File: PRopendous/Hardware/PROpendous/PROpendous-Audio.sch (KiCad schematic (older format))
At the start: 25 parts, among them M1 ELECTRET_MIC, U7 Video, U8 Headphones, U9 Line

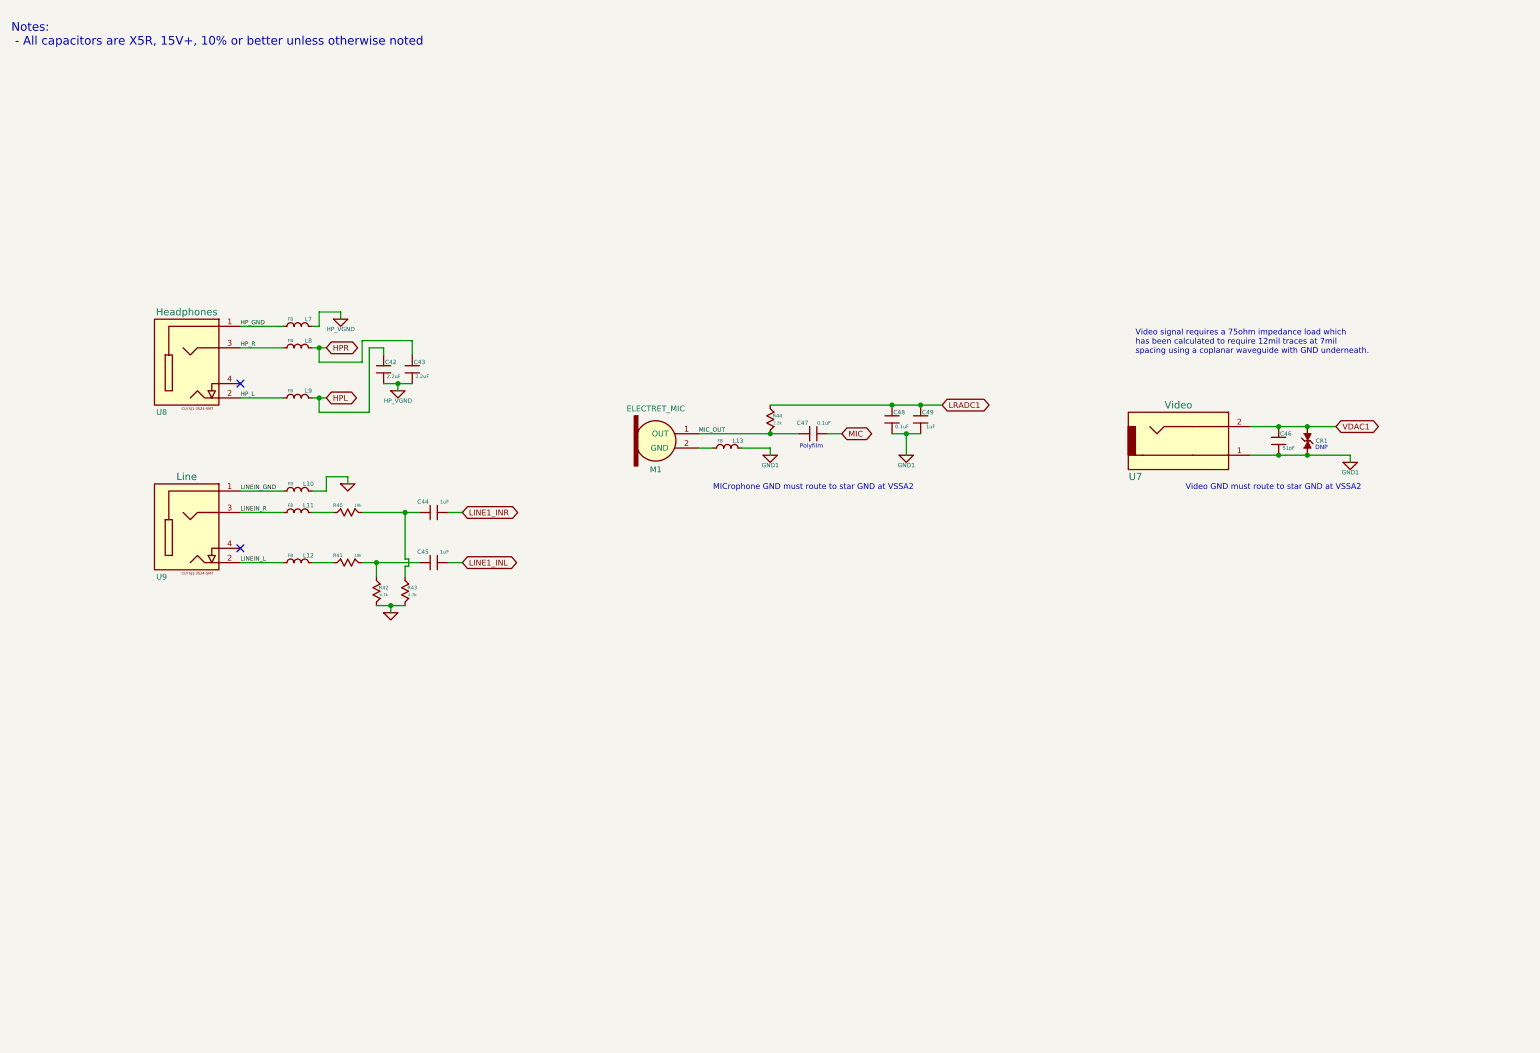
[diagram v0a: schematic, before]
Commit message: Updated PROpendous Project.  PCB layout is nearing completion.
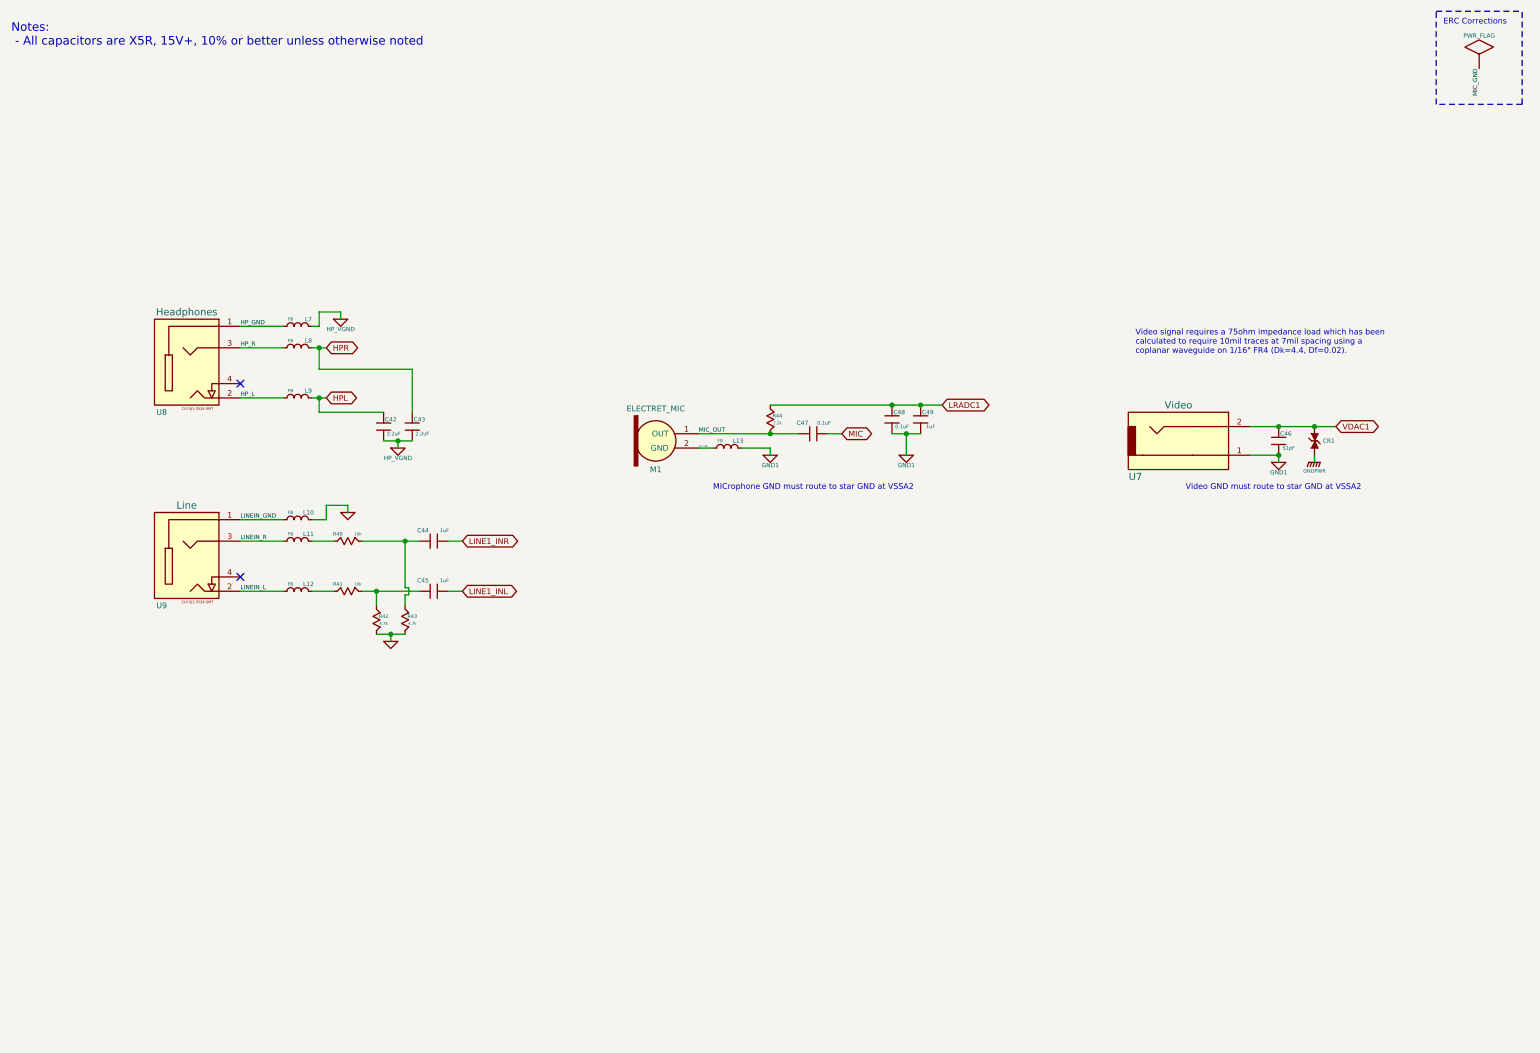
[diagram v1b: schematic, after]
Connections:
- net GND1: no longer CR1.1 (cathode)
- net MIC_GND: now reaches L13.2 (B), M1.2 (GND)
- new net GNDPWR: CR1.1 (cathode)
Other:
- note added: "ERC Corrections"
- note added: "Video signal requires a 75ohm impedance load which has been\ncalculated to require 10mil traces at 7mil spacing using a\ncoplanar waveguide on 1/16" FR4 (Dk=4.4, Df=0.02)."
- note removed: "DNP"
- note removed: "Polyfilm"
- note removed: "Video signal requires a 75ohm impedance load which\nhas been calculated to require 12mil traces at 7mil\nspacing using a coplanar waveguide with GND underneath."
- moved on the sheet: C42, C43, C44, C45, CR1, L10, L11, L12, R40, R41, R42, R43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

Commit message: First revision of i.MX233-based PROpendous board is complete.
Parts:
- added C79, C80: 0.1uF, symbol C_MINI
- added C81: 10uF, symbol C_MINI
- added IC7: MMA7455, symbol MMA745X
- added TP10: CONN_1, symbol CONN_1
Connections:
- net labels added: I2C_SCL-GPMI_RDY2-AUART1_TX, I2C_SDA-GPMI_CE2n-AUART1_RX, VDDIO_3V3
- wire segments 49 -> 60
- no-connect marks 2 -> 7
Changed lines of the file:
@@
-EESchema Schematic File Version 2  date 25/04/2010 07:03:32
+EESchema Schematic File Version 2  date 26/04/2010 13:13:01
 LIBS:opendous
 LIBS:device
@@
 Sheet 6 8
 Title "PROpendous"
-Date "25 apr 2010"
+Date "26 apr 2010"
 Rev "1.0"
 Comp "Opendous Inc. (www.opendous.org)"
@@
 Comment4 "www.PROpendous.org"
 $EndDescr
-Wire Wire Line
-	3450 3300 3450 3000
-Wire Wire Line
-	3450 3000 2800 3000
-Connection ~ 2800 2850
-Wire Wire Line
-	2800 3000 2800 2850
+Text GLabel 6600 7650 2    40   BiDi ~ 0
+MIC_OUT
+Text GLabel 6600 7550 2    40   BiDi ~ 0
+MIC_GND
+Text Label 6600 7550 2    30   ~ 0
+MIC_GND
+Text Label 6600 7650 2    30   ~ 0
+MIC_OUT
+Wire Wire Line
+	6150 6250 6050 6250
+Connection ~ 5350 5800
+Wire Wire Line
+	6050 6100 6050 5800
+Wire Wire Line
+	5300 7250 5300 7300
+Wire Wire Line
+	5250 6700 5350 6700
+Wire Wire Line
+	5300 6700 5300 6750
+Connection ~ 5300 6700
+Wire Wire Line
+	5300 5800 5300 5750
+Connection ~ 5300 5800
+Wire Wire Line
+	5500 7050 5100 7050
+Connection ~ 5300 7050
+Wire Wire Line
+	5500 7250 5100 7250
+Connection ~ 5300 7250
+Wire Wire Line
+	5300 7000 5300 7050
+Connection ~ 2800 3200
+Wire Wire Line
+	3250 3300 2800 3300
+Wire Wire Line
+	2800 3300 2800 3200
+Connection ~ 9750 3400
+Wire Wire Line
+	9300 3400 9900 3400
+Connection ~ 9500 3600
+Wire Wire Line
+	9500 3650 9500 3600
+Connection ~ 6800 3250
+Wire Wire Line
+	7150 3250 5950 3250
+Wire Wire Line
+	7000 3450 6800 3450
+Wire Wire Line
+	5550 3550 5450 3550
+Connection ~ 5950 3450
+Wire Wire Line
+	5450 3450 6150 3450
+Wire Wire Line
+	9500 3600 9300 3600
+Wire Wire Line
+	3700 4550 3800 4550
+Connection ~ 3300 4850
+Wire Wire Line
+	3300 4900 3300 4850
+Wire Wire Line
+	3000 4000 3000 3950
+Wire Wire Line
+	3000 3950 2850 3950
+Wire Wire Line
+	2850 3950 2850 4050
+Wire Wire Line
+	2850 4050 2750 4050
+Connection ~ 3200 4550
+Wire Wire Line
+	3200 4650 3200 4550
+Wire Wire Line
+	3500 4200 3100 4200
+Wire Wire Line
+	2750 4200 2900 4200
+Wire Wire Line
+	2250 4050 2550 4050
+Wire Wire Line
+	2250 4550 2550 4550
+Wire Wire Line
+	2850 2850 2750 2850
+Connection ~ 3350 3500
+Wire Wire Line
+	3350 3550 3350 3500
+Wire Wire Line
+	2250 3200 2550 3200
+Wire Wire Line
+	2250 2700 2550 2700
+Wire Wire Line
+	2250 2850 2550 2850
+Wire Wire Line
+	3250 3500 3450 3500
+Wire Wire Line
+	2750 2700 2800 2700
+Wire Wire Line
+	2800 2700 2800 2600
+Wire Wire Line
+	2800 2600 2950 2600
+Wire Wire Line
+	2950 2600 2950 2650
+Wire Wire Line
+	2750 3200 2850 3200
+Wire Wire Line
+	2550 4200 2250 4200
+Wire Wire Line
+	2750 4550 2900 4550
+Wire Wire Line
+	3500 4550 3100 4550
+Wire Wire Line
+	3400 4200 3400 4525
+Connection ~ 3400 4200
+Wire Wire Line
+	3400 4525 3425 4525
+Wire Wire Line
+	3425 4525 3425 4575
+Wire Wire Line
+	3425 4575 3400 4575
+Wire Wire Line
+	3400 4575 3400 4650
+Wire Wire Line
+	3200 4850 3400 4850
+Wire Wire Line
+	3700 4200 3800 4200
+Wire Wire Line
+	6450 3450 6350 3450
+Wire Wire Line
+	5750 3550 5950 3550
+Wire Wire Line
+	5950 3550 5950 3600
+Wire Wire Line
+	6900 3600 6900 3450
+Connection ~ 6900 3450
+Connection ~ 7000 3250
+Wire Wire Line
+	9750 3650 9750 3600
+Connection ~ 9500 3400
+Wire Notes Line
+	10600 500  11200 500
+Wire Notes Line
+	10600 500  10600 1150
+Wire Notes Line
+	10600 1150 11200 1150
 Wire Notes Line
 	11200 1150 11200 500
-Wire Notes Line
-	11200 1150 10600 1150
-Wire Notes Line
-	10600 1150 10600 500
-Wire Notes Line
-	10600 500  11200 500
-Connection ~ 9500 3400
-Wire Wire Line
-	9750 3650 9750 3600
-Connection ~ 7000 3250
-Connection ~ 6900 3450
-Wire Wire Line
-	6900 3600 6900 3450
-Wire Wire Line
-	5950 3600 5950 3550
-Wire Wire Line
-	5950 3550 5750 3550
-Wire Wire Line
-	6450 3450 6350 3450
-Wire Wire Line
-	3700 4200 3800 4200
-Wire Wire Line
-	3200 4850 3400 4850
-Wire Wire Line
-	3400 4650 3400 4575
-Wire Wire Line
-	3400 4575 3425 4575
-Wire Wire Line
-	3425 4575 3425 4525
-Wire Wire Line
-	3425 4525 3400 4525
-Connection ~ 3400 4200
-Wire Wire Line
-	3400 4525 3400 4200
-Wire Wire Line
-	3500 4550 3100 4550
-Wire Wire Line
-	2750 4550 2900 4550
-Wire Wire Line
-	2550 4200 2250 4200
-Wire Wire Line
-	2750 3200 2850 3200
-Wire Wire Line
-	2950 2650 2950 2600
-Wire Wire Line
-	2950 2600 2800 2600
-Wire Wire Line
-	2800 2600 2800 2700
-Wire Wire Line
-	2800 2700 2750 2700
-Wire Wire Line
-	3250 3500 3450 3500
-Wire Wire Line
-	2250 2850 2550 2850
-Wire Wire Line
-	2250 2700 2550 2700
-Wire Wire Line
-	2250 3200 2550 3200
-Wire Wire Line
-	3350 3550 3350 3500
-Connection ~ 3350 3500
-Wire Wire Line
-	2850 2850 2750 2850
-Wire Wire Line
-	2250 4550 2550 4550
-Wire Wire Line
-	2250 4050 2550 4050
-Wire Wire Line
-	2750 4200 2900 4200
-Wire Wire Line
-	3500 4200 3100 4200
-Wire Wire Line
-	3200 4650 3200 4550
-Connection ~ 3200 4550
-Wire Wire Line
-	2750 4050 2850 4050
-Wire Wire Line
-	2850 4050 2850 3950
-Wire Wire Line
-	2850 3950 3000 3950
-Wire Wire Line
-	3000 3950 3000 4000
-Wire Wire Line
-	3300 4900 3300 4850
-Connection ~ 3300 4850
-Wire Wire Line
-	3700 4550 3800 4550
-Wire Wire Line
-	9300 3600 9500 3600
-Wire Wire Line
-	5450 3450 6150 3450
-Connection ~ 5950 3450
-Wire Wire Line
-	5550 3550 5450 3550
-Wire Wire Line
-	7000 3450 6800 3450
-Wire Wire Line
-	7150 3250 5950 3250
-Connection ~ 6800 3250
-Wire Wire Line
-	9500 3600 9500 3650
-Connection ~ 9500 3600
-Wire Wire Line
-	9300 3400 9900 3400
-Connection ~ 9750 3400
-Wire Wire Line
-	2800 3200 2800 3300
-Wire Wire Line
-	2800 3300 3250 3300
-Connection ~ 2800 3200
+Wire Wire Line
+	2800 2850 2800 3000
+Connection ~ 2800 2850
+Wire Wire Line
+	2800 3000 3450 3000
+Wire Wire Line
+	3450 3000 3450 3300
+Wire Wire Line
+	4550 6100 4550 5800
+Wire Wire Line
+	4550 5800 6050 5800
+Connection ~ 5250 5800
+$Comp
+L CONN_1 TP10
+U 1 1 4BD554E0
+P 6300 6250
+F 0 "TP10" H 6380 6250 40  0000 L CNN
+F 1 "CONN_1" H 6300 6305 30  0001 C CNN
+	1    6300 6250
+	1    0    0    -1
+$EndComp
+NoConn ~ 6050 6350
+NoConn ~ 4550 6200
 Text Notes 10650 600  0    40   ~ 0
 ERC Corrections
 $Comp
-L PWR_FLAG #FLG079
+L PWR_FLAG #FLG080
 U 1 1 4BD12A58
 P 10900 900
-F 0 "#FLG079" H 10900 1170 30  0001 C CNN
+F 0 "#FLG080" H 10900 1170 30  0001 C CNN
 F 1 "PWR_FLAG" H 10900 1130 30  0000 C CNN
 	1    10900 900
@@
 MIC_GND
 $Comp
-L GNDPWR #PWR080
+L GNDPWR #PWR081
 U 1 1 4BCE7D97
 P 9750 3650
-F 0 "#PWR080" H 9750 3700 40  0001 C CNN
+F 0 "#PWR081" H 9750 3700 40  0001 C CNN
 F 1 "GNDPWR" H 9750 3590 25  0000 C CNN
 	1    9750 3650
@@
 MIC_OUT
 $Comp
-L GND1 #PWR081
+L GND1 #PWR082
 U 1 1 4BCCE387
 P 6900 3600
-F 0 "#PWR081" H 6900 3600 30  0001 C CNN
+F 0 "#PWR082" H 6900 3600 30  0001 C CNN
 F 1 "GND1" H 6900 3530 30  0000 C CNN
 	1    6900 3600
@@
 Video GND must route to star GND at VSSA2
 $Comp
-L GND1 #PWR082
+L GND1 #PWR083
 U 1 1 4BCCDA66
 P 9500 3650
-F 0 "#PWR082" H 9500 3650 30  0001 C CNN
+F 0 "#PWR083" H 9500 3650 30  0001 C CNN
 F 1 "GND1" H 9500 3580 30  0000 C CNN
 	1    9500 3650
@@
 $EndComp
 $Comp
-L GND #PWR083
+L GND #PWR084
 U 1 1 4BCCD9E6
 P 3000 4000
-F 0 "#PWR083" H 3000 4000 30  0001 C CNN
+F 0 "#PWR084" H 3000 4000 30  0001 C CNN
 F 1 "GND" H 3000 3930 30  0001 C CNN
 	1    3000 4000
@@
 $EndComp
 $Comp
-L GND #PWR084
+L GND #PWR085
 U 1 1 4BCCD9E1
 P 3300 4900
-F 0 "#PWR084" H 3300 4900 30  0001 C CNN
+F 0 "#PWR085" H 3300 4900 30  0001 C CNN
 F 1 "GND" H 3300 4830 30  0001 C CNN
 	1    3300 4900
@@
 $EndComp
 $Comp
-L HP_VGND #PWR085
+L HP_VGND #PWR086
 U 1 1 4BCCD842
 P 2950 2650
-F 0 "#PWR085" H 2950 2650 30  0001 C CNN
+F 0 "#PWR086" H 2950 2650 30  0001 C CNN
 F 1 "HP_VGND" H 2950 2580 30  0000 C CNN
 	1    2950 2650
@@
 $EndComp
 $Comp
-L HP_VGND #PWR086
+L HP_VGND #PWR087
 U 1 1 4BCCD77B
 P 3350 3550
-F 0 "#PWR086" H 3350 3550 30  0001 C CNN
+F 0 "#PWR087" H 3350 3550 30  0001 C CNN
 F 1 "HP_VGND" H 3350 3480 30  0000 C CNN
 	1    3350 3550
@@
 HP_GND
 $Comp
-L GND1 #PWR087
+L GND1 #PWR088
 U 1 1 4BCCBBD7
 P 5950 3600
-F 0 "#PWR087" H 5950 3600 30  0001 C CNN
+F 0 "#PWR088" H 5950 3600 30  0001 C CNN
 F 1 "GND1" H 5950 3530 30  0000 C CNN
 	1    5950 3600
@@
 Text GLabel 7150 3250 2    40   BiDi ~ 0
 LRADC1
+$Comp
+L VDDIO_3V3 #PWR089
+U 1 1 4BD552F5
+P 5300 7000
+F 0 "#PWR089" H 5300 7100 30  0001 C CNN
+F 1 "VDDIO_3V3" H 5300 7100 30  0000 C CNN
+	1    5300 7000
+	1    0    0    -1
+$EndComp
+$Comp
+L GND #PWR090
+U 1 1 4BD552F1
+P 5300 7300
+F 0 "#PWR090" H 5300 7300 30  0001 C CNN
+F 1 "GND" H 5300 7230 30  0001 C CNN
+	1    5300 7300
+	1    0    0    -1
+$EndComp
+$Comp
+L C_MINI C81
+U 1 1 4BD552D3
+P 5500 7150
+F 0 "C81" V 5450 7200 30  0000 C CNN
+F 1 "10uF" V 5550 7220 25  0000 C CNN
+	1    5500 7150
+	0    1    1    0
+$EndComp
+$Comp
+L C_MINI C80
+U 1 1 4BD552D0
+P 5300 7150
+F 0 "C80" V 5250 7200 30  0000 C CNN
+F 1 "0.1uF" V 5350 7220 25  0000 C CNN
+	1    5300 7150
+	0    1    1    0
+$EndComp
+$Comp
+L C_MINI C79
+U 1 1 4BD552CB
+P 5100 7150
+F 0 "C79" V 5050 7200 30  0000 C CNN
+F 1 "0.1uF" V 5150 7220 25  0000 C CNN
+	1    5100 7150
+	0    1    1    0
+$EndComp
+Text GLabel 4550 6300 0    40   BiDi ~ 0
+I2C_SDA-GPMI_CE2n-AUART1_RX
+Text GLabel 4550 6400 0    40   BiDi ~ 0
+I2C_SCL-GPMI_RDY2-AUART1_TX
+NoConn ~ 5600 6550
+NoConn ~ 5550 6550
+NoConn ~ 5500 6550
+$Comp
+L GND #PWR091
+U 1 1 4BD5527B
+P 5300 6750
+F 0 "#PWR091" H 5300 6750 30  0001 C CNN
+F 1 "GND" H 5300 6680 30  0001 C CNN
+	1    5300 6750
+	1    0    0    -1
+$EndComp
+$Comp
+L VDDIO_3V3 #PWR092
+U 1 1 4BD55273
+P 5300 5750
+F 0 "#PWR092" H 5300 5850 30  0001 C CNN
+F 1 "VDDIO_3V3" H 5300 5850 30  0000 C CNN
+	1    5300 5750
+	1    0    0    -1
+$EndComp
+$Comp
+L MMA745X IC7
+U 1 1 4BD551F4
+P 5300 6250
+F 0 "IC7" H 4850 5950 60  0000 C CNN
+F 1 "MMA7455" H 4950 6550 50  0000 C CNN
+	1    5300 6250
+	1    0    0    -1
+$EndComp
 $EndSCHEMATC

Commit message: Updated i.MX233-based PROpendous board with EEPROM to fix Freescale Errata #2229.
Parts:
- C42, C43: value 2.2uF -> 2.2nF
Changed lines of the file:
@@
-EESchema Schematic File Version 2  date 26/04/2010 13:13:01
+EESchema Schematic File Version 2  date 27/04/2010 18:25:33
 LIBS:opendous
 LIBS:device
@@
 Sheet 6 8
 Title "PROpendous"
-Date "26 apr 2010"
+Date "27 apr 2010"
 Rev "1.0"
 Comp "Opendous Inc. (www.opendous.org)"
@@
 ERC Corrections
 $Comp
-L PWR_FLAG #FLG080
+L PWR_FLAG #FLG082
 U 1 1 4BD12A58
 P 10900 900
-F 0 "#FLG080" H 10900 1170 30  0001 C CNN
+F 0 "#FLG082" H 10900 1170 30  0001 C CNN
 F 1 "PWR_FLAG" H 10900 1130 30  0000 C CNN
 	1    10900 900
@@
 MIC_GND
 $Comp
-L GNDPWR #PWR081
+L GNDPWR #PWR083
 U 1 1 4BCE7D97
 P 9750 3650
-F 0 "#PWR081" H 9750 3700 40  0001 C CNN
+F 0 "#PWR083" H 9750 3700 40  0001 C CNN
 F 1 "GNDPWR" H 9750 3590 25  0000 C CNN
 	1    9750 3650
@@
 MIC_OUT
 $Comp
-L GND1 #PWR082
+L GND1 #PWR084
 U 1 1 4BCCE387
 P 6900 3600
-F 0 "#PWR082" H 6900 3600 30  0001 C CNN
+F 0 "#PWR084" H 6900 3600 30  0001 C CNN
 F 1 "GND1" H 6900 3530 30  0000 C CNN
 	1    6900 3600
@@
 Video GND must route to star GND at VSSA2
 $Comp
-L GND1 #PWR083
+L GND1 #PWR085
 U 1 1 4BCCDA66
 P 9500 3650
-F 0 "#PWR083" H 9500 3650 30  0001 C CNN
+F 0 "#PWR085" H 9500 3650 30  0001 C CNN
 F 1 "GND1" H 9500 3580 30  0000 C CNN
 	1    9500 3650
@@
 $EndComp
 $Comp
-L GND #PWR084
+L GND #PWR086
 U 1 1 4BCCD9E6
 P 3000 4000
-F 0 "#PWR084" H 3000 4000 30  0001 C CNN
+F 0 "#PWR086" H 3000 4000 30  0001 C CNN
 F 1 "GND" H 3000 3930 30  0001 C CNN
 	1    3000 4000
@@
 $EndComp
 $Comp
-L GND #PWR085
+L GND #PWR087
 U 1 1 4BCCD9E1
 P 3300 4900
-F 0 "#PWR085" H 3300 4900 30  0001 C CNN
+F 0 "#PWR087" H 3300 4900 30  0001 C CNN
 F 1 "GND" H 3300 4830 30  0001 C CNN
 	1    3300 4900
@@
 $EndComp
 $Comp
-L HP_VGND #PWR086
+L HP_VGND #PWR088
 U 1 1 4BCCD842
 P 2950 2650
-F 0 "#PWR086" H 2950 2650 30  0001 C CNN
+F 0 "#PWR088" H 2950 2650 30  0001 C CNN
 F 1 "HP_VGND" H 2950 2580 30  0000 C CNN
 	1    2950 2650
@@
 $EndComp
 $Comp
-L HP_VGND #PWR087
+L HP_VGND #PWR089
 U 1 1 4BCCD77B
 P 3350 3550
-F 0 "#PWR087" H 3350 3550 30  0001 C CNN
+F 0 "#PWR089" H 3350 3550 30  0001 C CNN
 F 1 "HP_VGND" H 3350 3480 30  0000 C CNN
 	1    3350 3550
@@
 P 3450 3400
 F 0 "C43" V 3400 3450 30  0000 C CNN
-F 1 "2.2uF" V 3500 3470 25  0000 C CNN
+F 1 "2.2nF" V 3500 3470 25  0000 C CNN
 	1    3450 3400
 	0    1    1    0
@@
 P 3250 3400
 F 0 "C42" V 3200 3450 30  0000 C CNN
-F 1 "2.2uF" V 3300 3470 25  0000 C CNN
+F 1 "2.2nF" V 3300 3470 25  0000 C CNN
 	1    3250 3400
 	0    1    1    0
@@
 HP_GND
 $Comp
-L GND1 #PWR088
+L GND1 #PWR090
 U 1 1 4BCCBBD7
 P 5950 3600
-F 0 "#PWR088" H 5950 3600 30  0001 C CNN
+F 0 "#PWR090" H 5950 3600 30  0001 C CNN
 F 1 "GND1" H 5950 3530 30  0000 C CNN
 	1    5950 3600
@@
 LRADC1
 $Comp
-L VDDIO_3V3 #PWR089
+L VDDIO_3V3 #PWR091
 U 1 1 4BD552F5
 P 5300 7000
-F 0 "#PWR089" H 5300 7100 30  0001 C CNN
+F 0 "#PWR091" H 5300 7100 30  0001 C CNN
 F 1 "VDDIO_3V3" H 5300 7100 30  0000 C CNN
 	1    5300 7000
@@
 $EndComp
 $Comp
-L GND #PWR090
+L GND #PWR092
 U 1 1 4BD552F1
 P 5300 7300
-F 0 "#PWR090" H 5300 7300 30  0001 C CNN
+F 0 "#PWR092" H 5300 7300 30  0001 C CNN
 F 1 "GND" H 5300 7230 30  0001 C CNN
 	1    5300 7300
@@
 NoConn ~ 5500 6550
 $Comp
-L GND #PWR091
+L GND #PWR093
 U 1 1 4BD5527B
 P 5300 6750
-F 0 "#PWR091" H 5300 6750 30  0001 C CNN
+F 0 "#PWR093" H 5300 6750 30  0001 C CNN
 F 1 "GND" H 5300 6680 30  0001 C CNN
 	1    5300 6750
@@
 $EndComp
 $Comp
-L VDDIO_3V3 #PWR092
+L VDDIO_3V3 #PWR094
 U 1 1 4BD55273
 P 5300 5750
-F 0 "#PWR092" H 5300 5850 30  0001 C CNN
+F 0 "#PWR094" H 5300 5850 30  0001 C CNN
 F 1 "VDDIO_3V3" H 5300 5850 30  0000 C CNN
 	1    5300 5750
